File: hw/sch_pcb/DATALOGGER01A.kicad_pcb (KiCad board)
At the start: 2 copper layers, 80.8 x 101.1 mm, 90 parts, among them J1 HEADER_2x01_PARALLEL, J10 HEADER_2x03_PARALLEL, J11 HEADER_2x01, J12 HEADER_2x01_PARALLEL, J13 HEADER_2x01_PARALLEL, J14 HEADER_2x01_PARALLEL, J15 HEADER_2x01_PARALLEL, J16 HEADER_2x01_PARALLEL, J17 HEADER_2x01_PARALLEL, J18 HEADER_2x01_PARALLEL, J19 HEADER_2x01_PARALLEL, J2 HEADER_2x01_PARALLEL, J20 HEADER_2x01_PARALLEL, J21 HEADER_2x01, J22 HEADER_2x01_PARALLEL, J23 HEADER_2x01_PARALLEL, J24 HEADER_2x01_PARALLEL, J25 HEADER_2x01_PARALLEL, J26 HEADER_2x01_PARALLEL, J27 HEADER_2x01_PARALLEL, J28 HEADER_2x01_PARALLEL, J29 HEADER_2x01_PARALLEL, J3 HEADER_2x01_PARALLEL, J30 HEADER_2x01_PARALLEL, J31 HEADER_2x03, J32 HEADER_2x01, J33 HEADER_2x03_PARALLEL, J34 MCC-SD (kouka z modulu), J4 HEADER_2x01_PARALLEL, J5 HEADER_2x01_PARALLEL, J6 HEADER_2x03_PARALLEL, J7 MCC-SD, J8 HEADER_2x01_PARALLEL, J9 HEADER_2x01, M2 HOLE, M3 HOLE, M4 HOLE, SW1 5MS1S102AM6QE, U1 ISL21080CIH320Z-TK, U2 TPS22965-Q1, U3 ATMEGA1284P-AU, U4 PCF85263A, U5 LM4041CIM3-1.2(neosazovat), U6 AT24CS64-SSHM, Y1 16MHz, Y2 ABS07-120-32.768KHZ-T

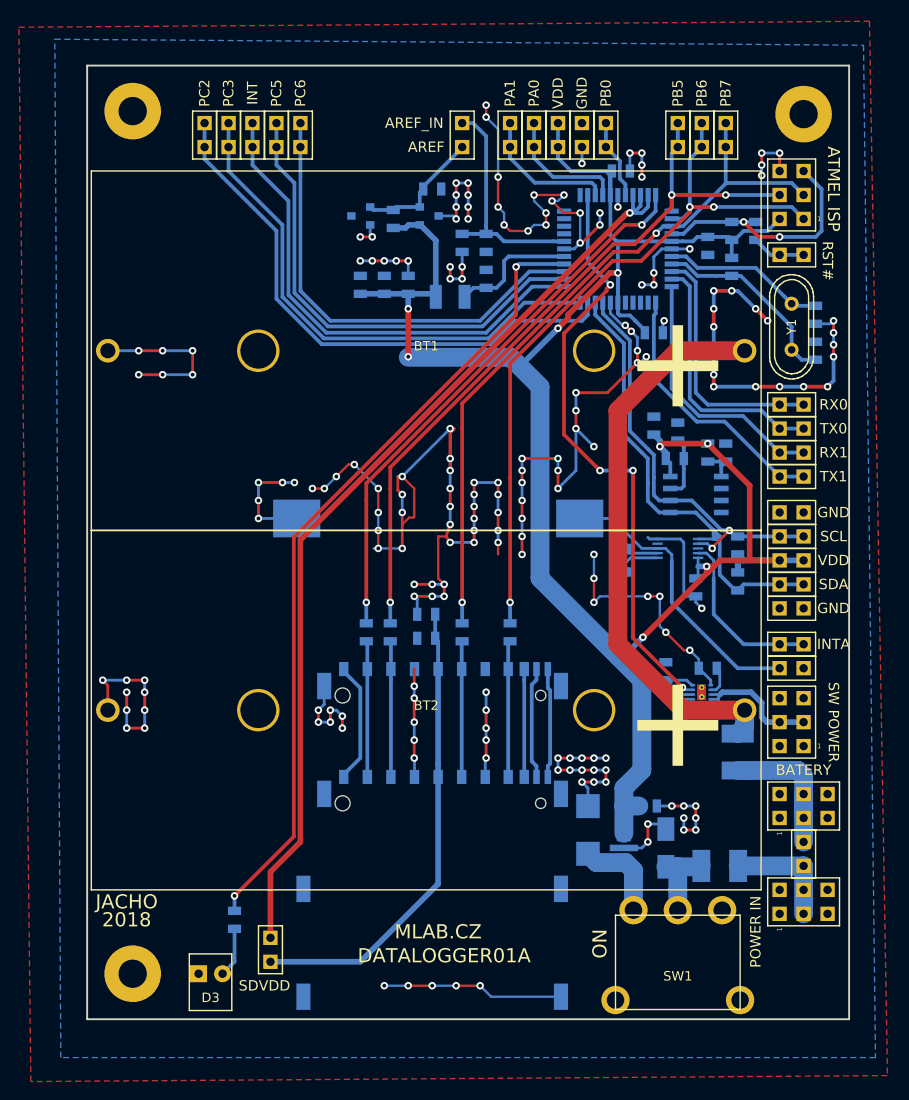
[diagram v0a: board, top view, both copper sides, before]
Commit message: Set up coordinates origin in left bottom corner of board.
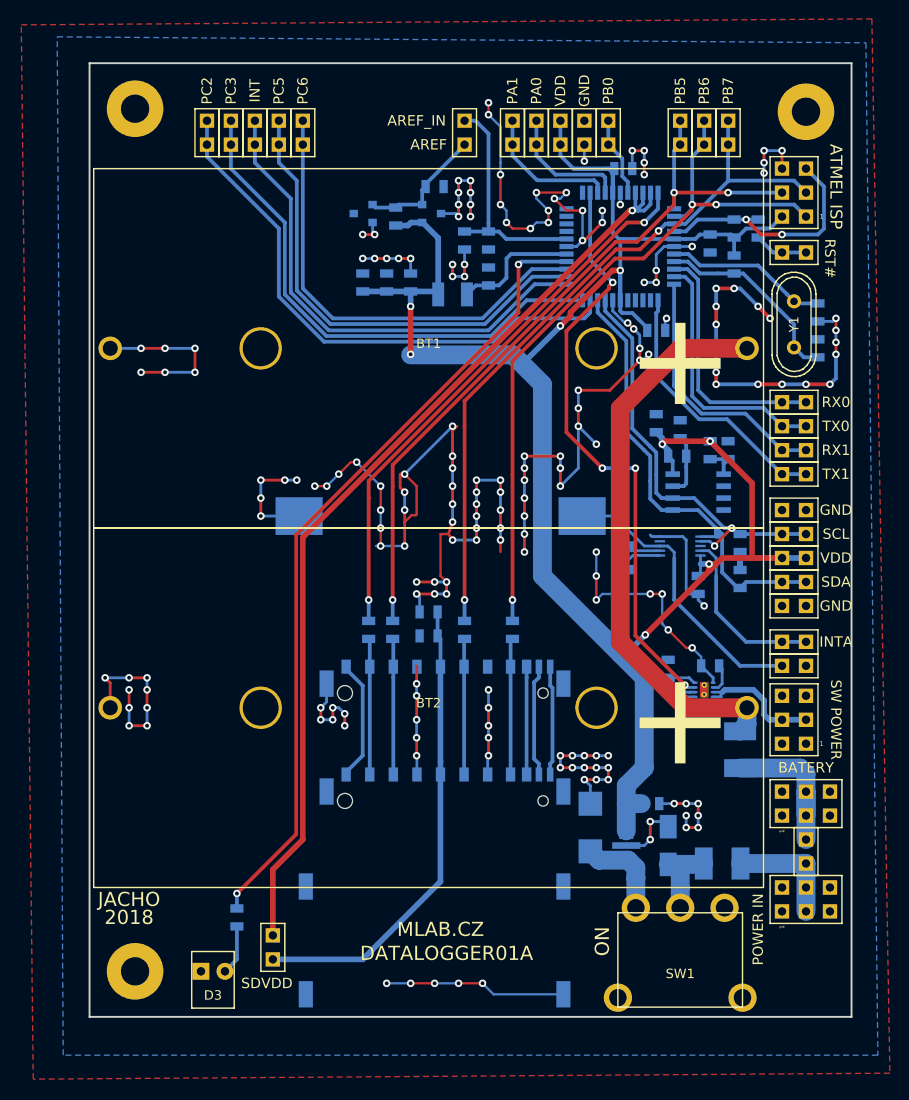
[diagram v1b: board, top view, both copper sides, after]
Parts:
- moved BT1 0.36 mm to (142.6, 76.8)
- moved C12 0.36 mm to (172.5, 110.5)
- moved C13 0.36 mm to (166.1, 125.1)
- moved C14 0.36 mm to (146.4, 65.4)
- moved C15 0.36 mm to (142.6, 107.3)
- moved C21 0.36 mm to (172.5, 65.7)
- moved C3 0.36 mm to (140.7, 69.8)
- moved R11 0.36 mm to (172.5, 87.6)
- moved R12 0.36 mm to (174.4, 87.6)
- moved J24 0.36 mm to (156.6, 54.0)
- moved J28 0.36 mm to (174.4, 54.0)
- moved J9 0.36 mm to (146.4, 54.0)
- moved U5 0.36 mm to (135.7, 62.5)
- moved BT2 0.36 mm to (142.6, 114.9)
- moved C10 0.36 mm to (163.6, 129.5)
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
